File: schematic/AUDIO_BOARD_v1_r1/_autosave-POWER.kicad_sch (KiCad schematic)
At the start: 10 parts, among them U20 DAC8565, U21 MCP23S17, U22 AP2112K-3.3

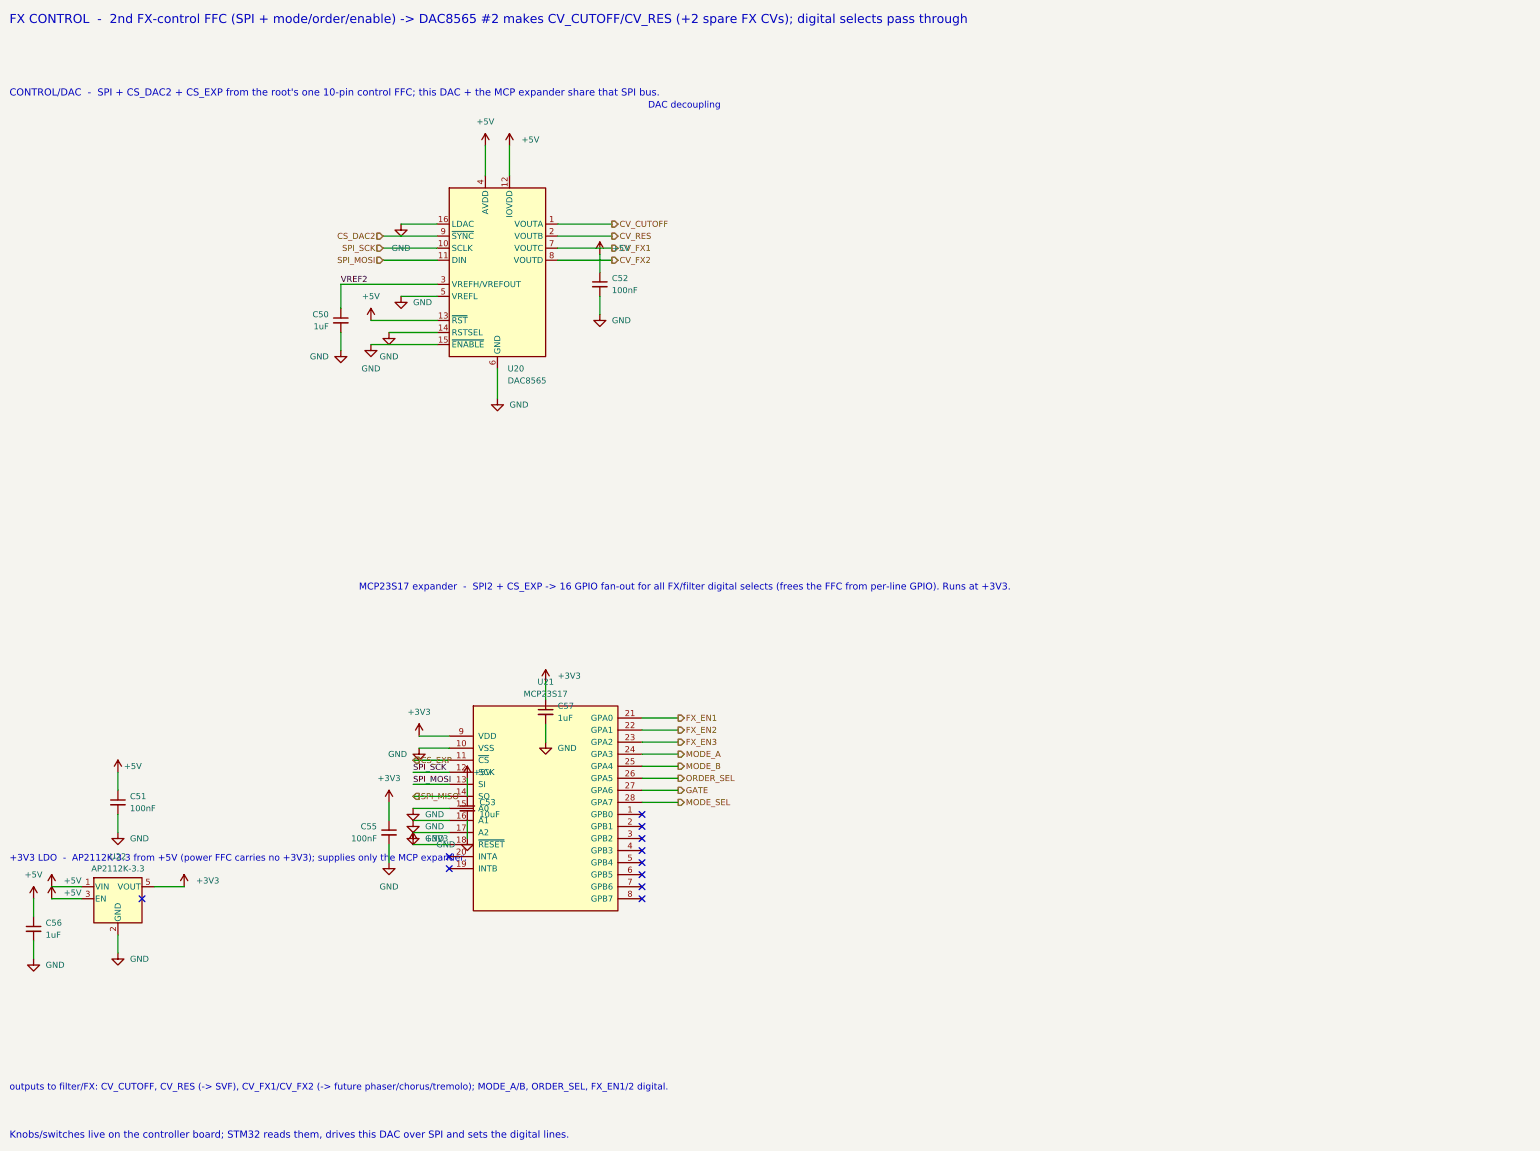
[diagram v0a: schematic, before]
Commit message: placement. start with each sheet for the most part
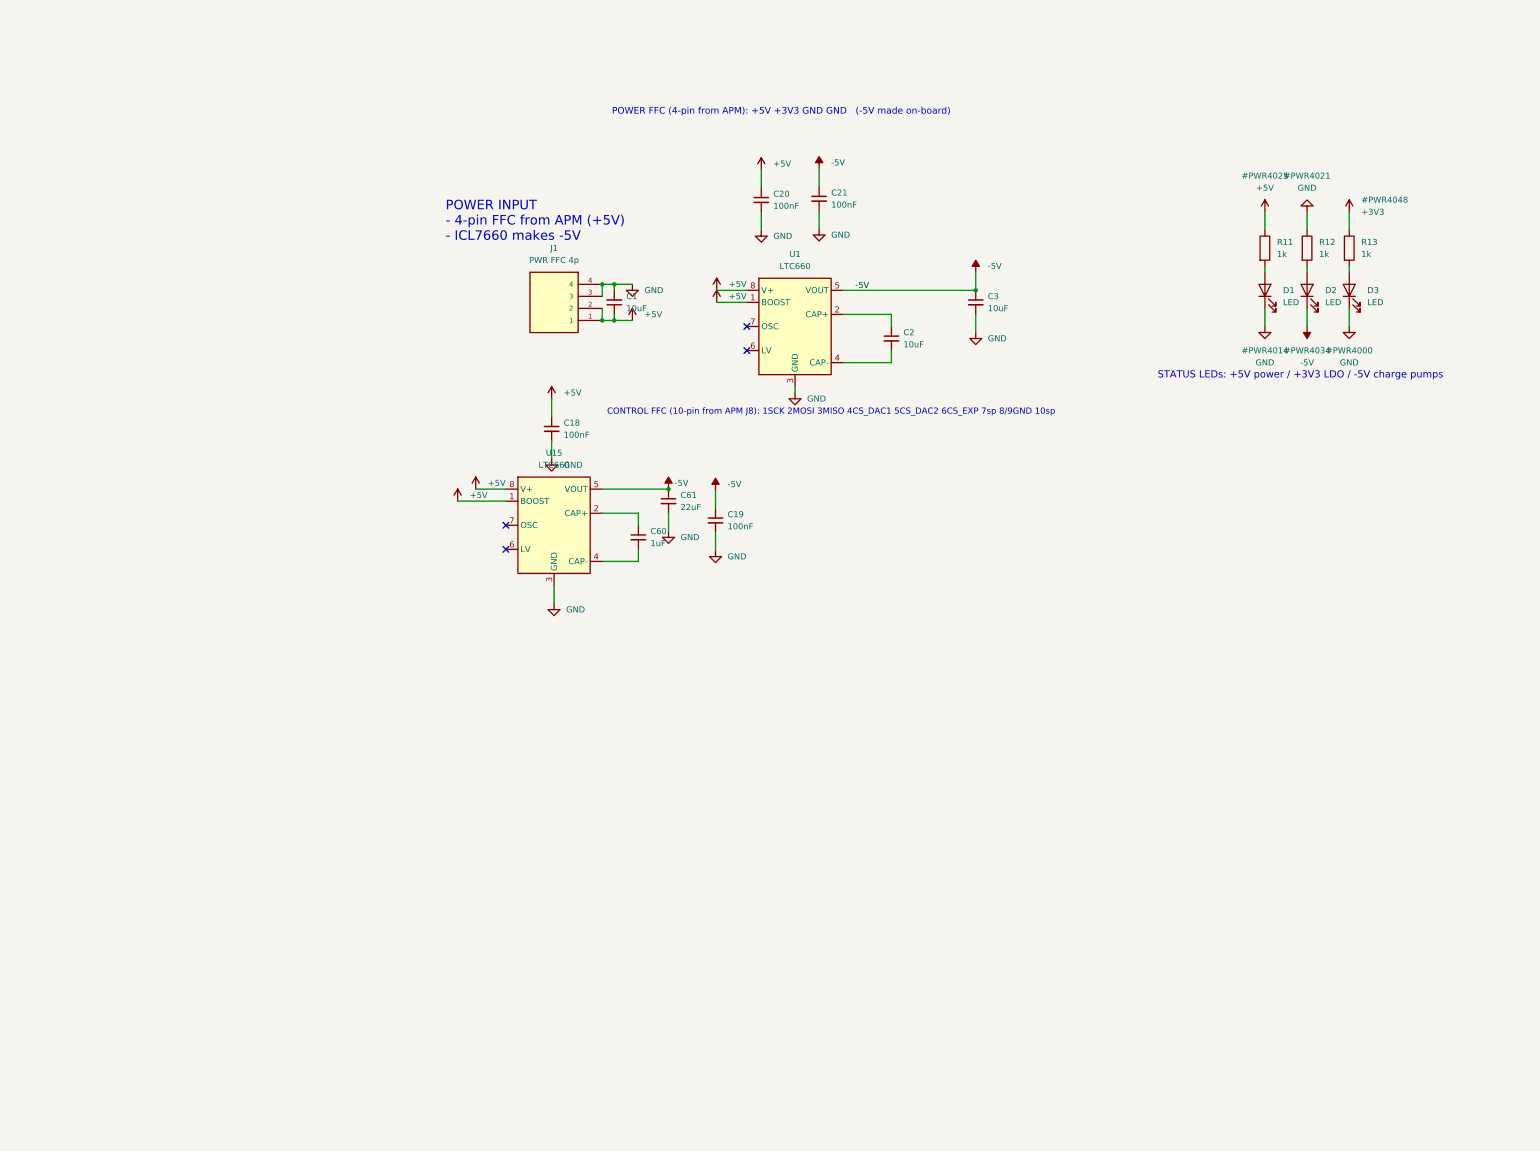
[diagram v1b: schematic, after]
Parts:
- removed C50, C56, C57: 1uF, Capacitor_SMD:C_0402_1005Metric, symbol Device:C_Small
- removed C51, C52, C55: 100nF, Capacitor_SMD:C_0402_1005Metric, symbol Device:C_Small
- removed C53: 10uF, Capacitor_SMD:C_0805_2012Metric, symbol Device:C_Small
- removed U20: DAC8565, Package_SO:TSSOP-16_4.4x5mm_P0.65mm, symbol Analog_DAC:DAC8565
- removed U21: MCP23S17, Package_SO:SOIC-28W_7.5x17.9mm_P1.27mm, symbol Custom:MCP23S17
- removed U22: AP2112K-3.3, Package_TO_SOT_SMD:SOT-23-5, symbol Regulator_Linear:AP2112K-3.3
- added C1, C2, C3: 10uF, Capacitor_SMD:C_0805_2012Metric, symbol Device:C_Small
- added C18, C19, C20, C21: 100nF, Capacitor_SMD:C_0402_1005Metric, symbol Device:C_Small
- added C60: 1uF, Capacitor_SMD:C_0805_2012Metric, symbol Device:C_Small
- added C61: 22uF, Capacitor_SMD:C_0805_2012Metric, symbol Device:C_Small
- added D1, D2, D3: LED, LED_SMD:LED_0603_1608Metric, symbol Device:LED
- added J1: PWR FFC 4p, my_footprints:AMPHENOL_F3311A7H121004E200, symbol F3311A7H121004E200:F3311A7H121004E200
- added R11, R12, R13: 1k, Resistor_SMD:R_0402_1005Metric, symbol Device:R
- added U1, U15: LTC660, Package_SO:SOIC-8_3.9x4.9mm_P1.27mm, symbol Regulator_SwitchedCapacitor:LTC660
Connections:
- net +3V3: now also R13.1
- net +5V: now also C1.1, C18.1, C20.1, J1.1, J1.2, R11.1, U1.1 (BOOST), U1.8 (V+), U15.1 (BOOST), U15.8 (V+)
- net GND: now also C1.2, C18.2, C19.2, C20.2, C21.2, C3.2, C61.2, D1.1 (K), D3.1 (K), J1.3, J1.4, R12.1, U1.3 (GND), U15.3 (GND)
- new net: C2.1, U1.2 (CAP+)
- new net: C2.2, U1.4 (CAP-)
- new net: D1.2 (A), R11.2
- new net: C60.1, U15.2 (CAP+)
- new net: C60.2, U15.4 (CAP-)
- new net: D2.2 (A), R12.2
- new net: D3.2 (A), R13.2
- new net -5V: C19.1, C21.1, C3.1, C61.1, D2.1 (K), U1.5 (VOUT), U15.5 (VOUT)
- no-connect marks 11 -> 4
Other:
- note added: "CONTROL FFC (10-pin from APM J8): 1SCK 2MOSI 3MISO 4CS_DAC1 5CS_DAC2 6CS_EXP 7sp 8/9GND 10sp"
- note added: "POWER FFC (4-pin from APM): +5V +3V3 GND GND (-5V made on-board)"
- note added: "POWER INPUT - 4-pin FFC from APM (+5V) - ICL7660 makes -5V"
- note added: "STATUS LEDs: +5V power / +3V3 LDO / -5V charge pumps"
- note removed: "+3V3 LDO - AP2112K-3.3 from +5V (power FFC carries no +3V3); supplies only the MCP expander."
- note removed: "CONTROL/DAC - SPI + CS_DAC2 + CS_EXP from the root's one 10-pin control FFC; this DAC + the MCP expander share that SPI bus."
- note removed: "DAC decoupling"
- note removed: "FX CONTROL - 2nd FX-control FFC (SPI + mode/order/enable) -> DAC8565 #2 makes CV_CUTOFF/CV_RES (+2 spare FX CVs); digital selects pass through"
- note removed: "Knobs/switches live on the controller board; STM32 reads them, drives this DAC over SPI and sets the digital lines."
- note removed: "MCP23S17 expander - SPI2 + CS_EXP -> 16 GPIO fan-out for all FX/filter digital selects (frees the FFC from per-line GPIO). Runs at +3V3."
- note removed: "outputs to filter/FX: CV_CUTOFF, CV_RES (-> SVF), CV_FX1/CV_FX2 (-> future phaser/chorus/tremolo); MODE_A/B, ORDER_SEL, FX_EN1/2 digital."
